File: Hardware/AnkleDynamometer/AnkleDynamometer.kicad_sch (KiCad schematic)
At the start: 16 parts, among them U1 INA129, U2 LT3080xMS8E, U3 ADS1220xPW

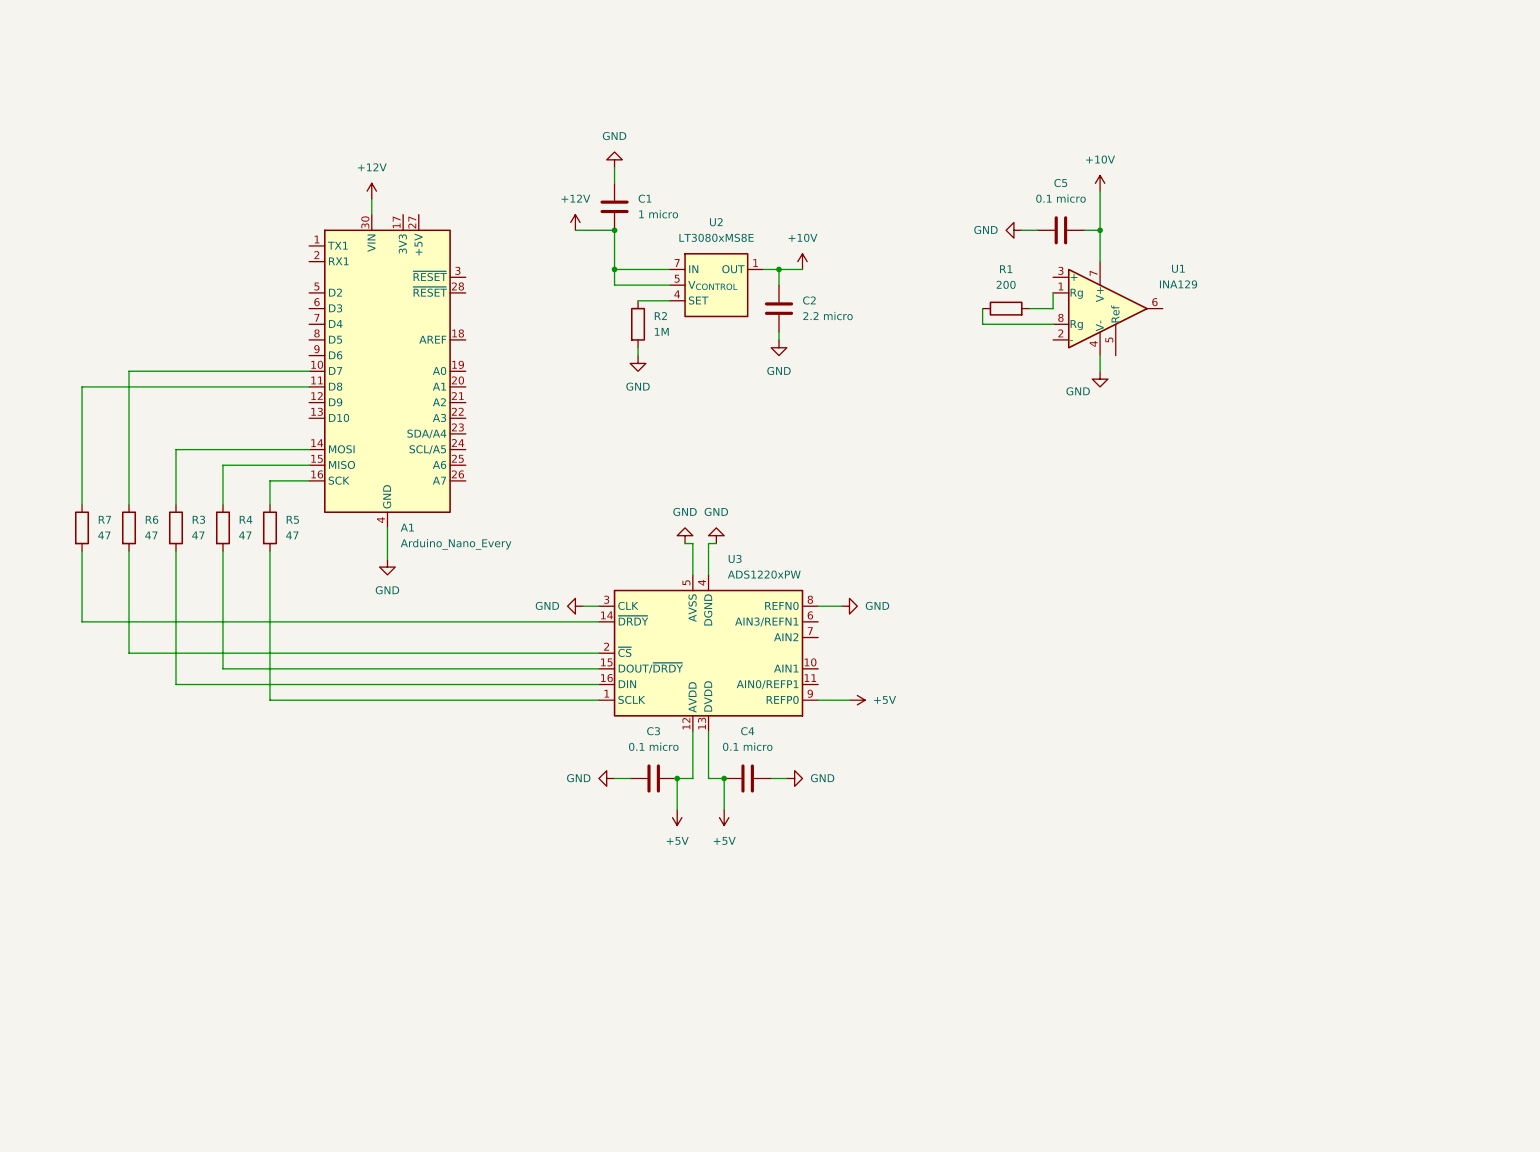
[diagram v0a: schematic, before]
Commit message: PCB Schematic
Put together the KiCAD schematic
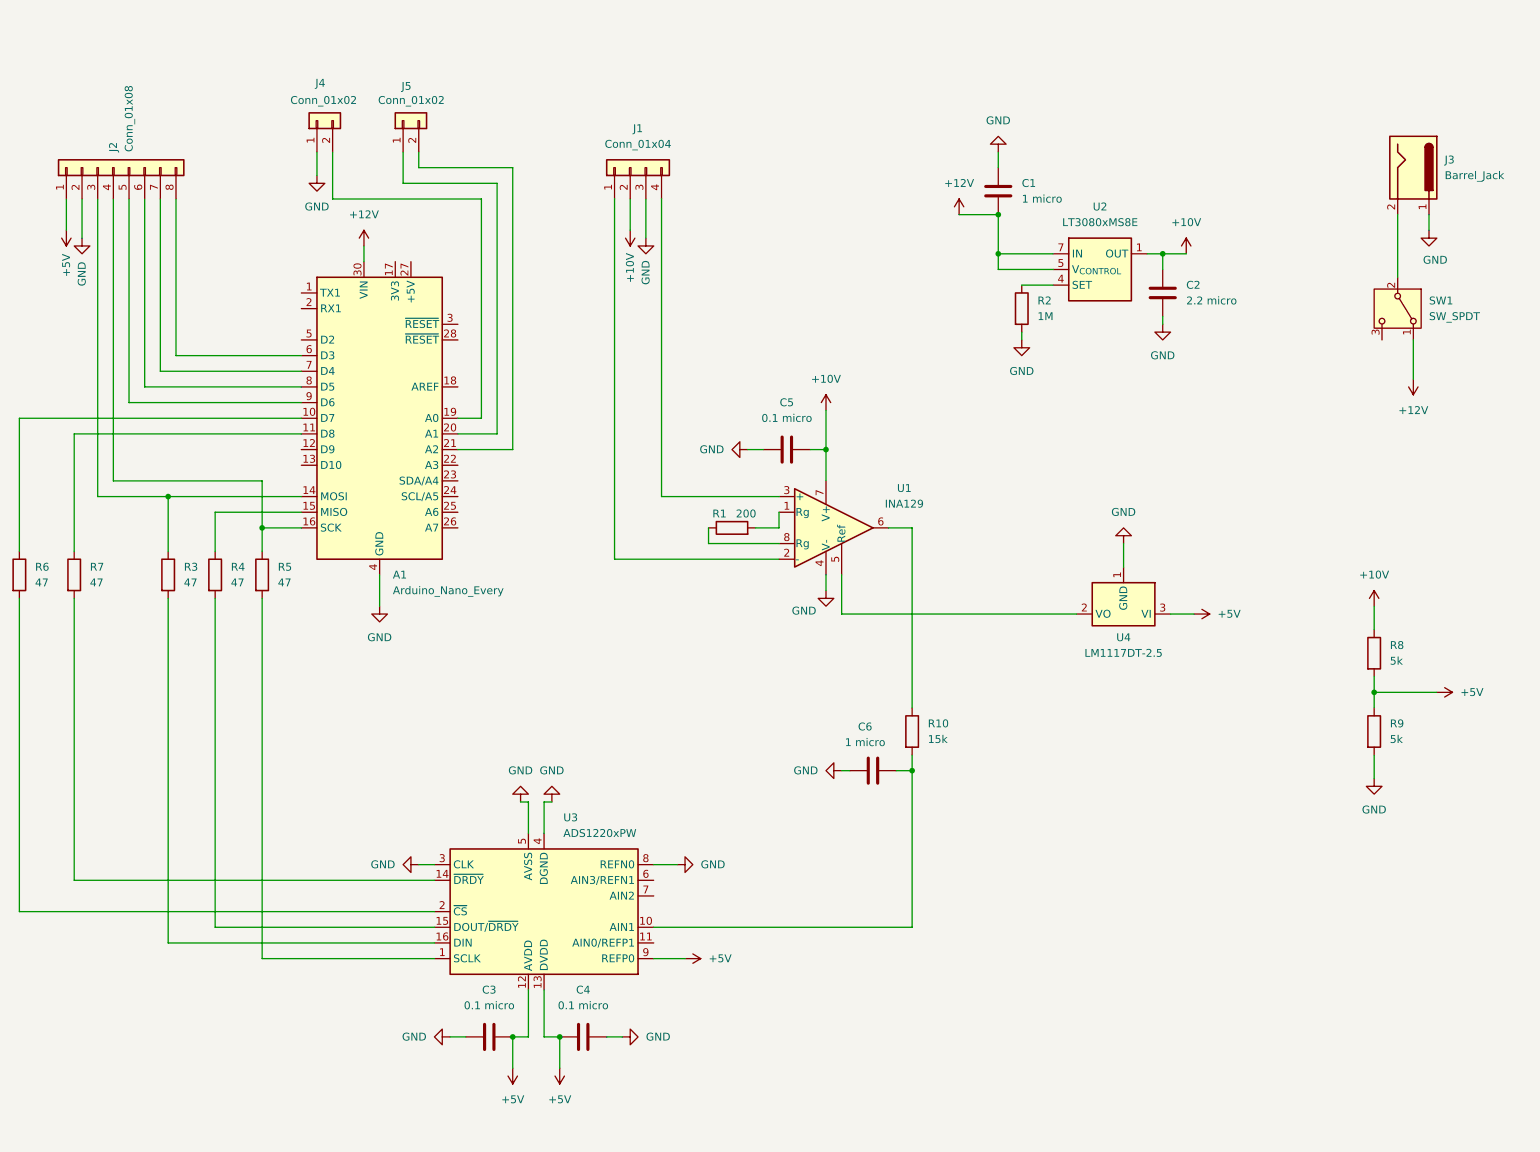
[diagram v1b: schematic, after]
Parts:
- added C6: 1 micro, symbol Device:C
- added J1: Conn_01x04, symbol Connector_Generic:Conn_01x04
- added J2: Conn_01x08, symbol Connector_Generic:Conn_01x08
- added J3: Barrel_Jack, symbol Connector:Barrel_Jack
- added J4, J5: Conn_01x02, symbol Connector_Generic:Conn_01x02
- added R10: 15k, symbol Device:R
- added R8, R9: 5k, symbol Device:R
- added SW1: SW_SPDT, symbol Switch:SW_SPDT
- added U4: LM1117DT-2.5, Package_TO_SOT_SMD:TO-252-3_TabPin2, symbol Regulator_Linear:LM1117DT-2.5
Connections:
- net +10V: now also J1.2 (Pin_2), R8.1
- net +12V: now also SW1.1 (A)
- net +5V: now also J2.1 (Pin_1), R8.2, R9.1, U4.3 (VI)
- net GND: now also C6.1, J1.3 (Pin_3), J2.2 (Pin_2), J3.1, J4.1 (Pin_1), R9.2, U4.1 (GND)
- net at A1.16 (SCK), R5.1: now also J2.4 (Pin_4)
- net at A1.14 (MOSI), R3.1: now also J2.3 (Pin_3)
- net at U3.10 (AIN1): now also C6.2, R10.2
- net at U1.2 (-): now also J1.1 (Pin_1)
- net at U1.3 (+): now also J1.4 (Pin_4)
- net at U1.5 (Ref): now also U4.2 (VO)
- net at U1.6: now also R10.1
- net at A1.19 (A0): now also J4.2 (Pin_2)
- net at A1.20 (A1): now also J5.1 (Pin_1)
- net at A1.21 (A2): now also J5.2 (Pin_2)
- net at A1.6 (D3): now also J2.8 (Pin_8)
- net at A1.7 (D4): now also J2.7 (Pin_7)
- net at A1.8 (D5): now also J2.6 (Pin_6)
- net at A1.9 (D6): now also J2.5 (Pin_5)
- new net: J3.2, SW1.2 (B)
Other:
- moved on the sheet: A1, C1, C2, C3, C4, C5, R1, R2, R3, R4, R5, R6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

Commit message: PCB
Updating schematic
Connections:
- net +5V: no longer C4.1, U3.13 (DVDD)
- net GND: now also C4.1; no longer C4.2
- net at A1.27 (+5V): now also C4.2, U3.13 (DVDD)
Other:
- moved on the sheet: C3, C4, C6, J1, R10, R3, R4, R5, U3

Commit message: PCB layout
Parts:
- removed U4: LM1117DT-2.5, Package_TO_SOT_SMD:TO-252-3_TabPin2, symbol Regulator_Linear:LM1117DT-2.5
- added C10, C11: 1 micro, Capacitor_SMD:C_0603_1608Metric, symbol Device:C
- added C7: 0.1 micro, Capacitor_SMD:C_0603_1608Metric, symbol Device:C
- added C8: 22 micro, Capacitor_Tantalum_SMD:CP_EIA-3216-18_Kemet-A, symbol Device:C_Polarized
- added C9: 10 micro, Capacitor_Tantalum_SMD:CP_EIA-3216-18_Kemet-A, symbol Device:C_Polarized
- added U5: AMS1117-2.5, Package_TO_SOT_SMD:SOT-223-3_TabPin2, symbol Regulator_Linear:AMS1117-2.5
- C1, C3, C4, C5: footprint (none) -> Capacitor_SMD:C_0603_1608Metric
- C2: footprint (none) -> Capacitor_SMD:C_0805_2012Metric
- C6: value 1 micro -> 10 nano; footprint (none) -> Capacitor_SMD:C_0603_1608Metric
- J1: footprint (none) -> Connector_JST:JST_EH_B4B-EH-A_1x04_P2.50mm_Vertical
- J2: footprint (none) -> Connector_JST:JST_EH_B8B-EH-A_1x08_P2.50mm_Vertical
- J3: footprint (none) -> Connector_BarrelJack:BarrelJack_Horizontal
- J4, J5: footprint (none) -> Connector_JST:JST_EH_B2B-EH-A_1x02_P2.50mm_Vertical
- R1, R2, R8, R9: footprint (none) -> Resistor_SMD:R_0805_2012Metric_Pad1.20x1.40mm_HandSolder
- R10: value 15k -> 1.5M; footprint (none) -> Resistor_SMD:R_0805_2012Metric_Pad1.20x1.40mm_HandSolder
- R3, R4, R5, R6, R7: footprint (none) -> Resistor_SMD:R_0603_1608Metric_Pad0.98x0.95mm_HandSolder
- SW1: footprint (none) -> SLW-121586-5A-D:SW_SLW-121586-5A-D
- U1: footprint (none) -> Package_DIP:DIP-8_W7.62mm
- U2: footprint Package_SO:MSOP-8-1EP_3x3mm_P0.65mm_EP1.68x1.88mm -> Package_TO_SOT_SMD:TO-263-5_TabPin3
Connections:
- net +10V: no longer U2.1 (OUT), U2.2 (OUT), U2.9 (OUT)
- net +12V: now also U2.4 (V_{CONTROL}); no longer U2.7 (IN), U2.8 (IN)
- net +5V: now also C3.1, C7.2, C9.1, U5.3 (VI); no longer C3.2, J2.1 (Pin_1)
- net GND: now also C3.2, J3.2, J5.1 (Pin_1), C10.1, C11.2, C7.1, C8.2, C9.2, U5.1 (GND); no longer C3.1, J3.1
- net at A1.27 (+5V), C4.2, U3.13 (DVDD): now also J2.1 (Pin_1)
- net at SW1.2 (B): now also J3.1; no longer J3.2
- net at A1.20 (A1): no longer J5.1 (Pin_1)
- net at J5.2 (Pin_2): now also A1.8 (D5); no longer A1.21 (A2)
- net at R2.1: now also U2.2 (SET), C11.1; no longer U2.4 (SET)
- net at R6.1: now also A1.22 (A3); no longer A1.10 (D7)
- net 2.5V: now reaches U1.5 (Ref)
- net 2.5V: now also C10.2, C8.1, U5.2 (VO)
- net at J1.1 (Pin_1): now also U1.3 (+); no longer U1.2 (-)
- net at J1.4 (Pin_4): now also U1.2 (-); no longer U1.3 (+)
- net at R7.1: now also A1.5 (D2); no longer A1.11 (D8)
- net at A1.12 (D9): now also J2.7 (Pin_7)
- net at A1.13 (D10): now also J2.8 (Pin_8)
- net at A1.19 (A0): no longer J4.2 (Pin_2)
- net at A1.6 (D3): no longer J2.8 (Pin_8)
- net at A1.7 (D4): no longer J2.7 (Pin_7)
- net at J2.6 (Pin_6): now also A1.11 (D8); no longer A1.8 (D5)
- net at J2.5 (Pin_5): now also A1.10 (D7); no longer A1.9 (D6)
- new net: A1.9 (D6), J4.2 (Pin_2)
- no-connect marks 0 -> 19
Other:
- moved on the sheet: C3, C4, C6, J4, J5, R10, R6, R7, SW1, U3

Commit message: PCB layout 2
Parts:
- added H1, H2, H3, H4: MountingHole, MountingHole:MountingHole_2.2mm_M2_Pad_Via, symbol Mechanical:MountingHole
- C1, C10, C11: value 1 micro -> 1u; footprint Capacitor_SMD:C_0603_1608Metric -> Capacitor_SMD:C_0805_2012Metric; LCSC (none) -> C28323
- C2: value 2.2 micro -> 2.2u; footprint Capacitor_SMD:C_0805_2012Metric -> Capacitor_SMD:C_1206_3216Metric; LCSC (none) -> C50254
- C3, C4, C5, C7: value 0.1 micro -> 100n; LCSC (none) -> C14663
- C6: value 10 nano -> 10n; LCSC (none) -> C85973
- C8: value 22 micro -> 22u; LCSC (none) -> C11366
- C9: value 10 micro -> 10u; LCSC (none) -> C7171
- R1: footprint Resistor_SMD:R_0805_2012Metric_Pad1.20x1.40mm_HandSolder -> Resistor_SMD:R_0603_1608Metric_Pad0.98x0.95mm_HandSolder; LCSC (none) -> C8218
- R10: footprint Resistor_SMD:R_0805_2012Metric_Pad1.20x1.40mm_HandSolder -> Resistor_SMD:R_0603_1608Metric_Pad0.98x0.95mm_HandSolder; LCSC (none) -> C137773
- R2: footprint Resistor_SMD:R_0805_2012Metric_Pad1.20x1.40mm_HandSolder -> Resistor_SMD:R_0603_1608Metric_Pad0.98x0.95mm_HandSolder; LCSC (none) -> C22935
- R3, R4, R5, R6, R7: LCSC (none) -> C23182
- R8, R9: value 5k -> 5.1k; footprint Resistor_SMD:R_0805_2012Metric_Pad1.20x1.40mm_HandSolder -> Resistor_SMD:R_0603_1608Metric_Pad0.98x0.95mm_HandSolder; LCSC (none) -> C23186
- U2: LCSC (none) -> C580029
- U3: LCSC (none) -> C48263
- U5: LCSC (none) -> C12087
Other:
- moved on the sheet: A1, C1, C10, C11, C2, C3, C4, C5, C6, C7, C8, C9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
